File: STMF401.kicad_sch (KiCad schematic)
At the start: 26 parts, among them J6 Conn_01x04_Pin, U7 STM32F407VETx, Y1 X322525MQB4SI, Y2 SMD03215C2

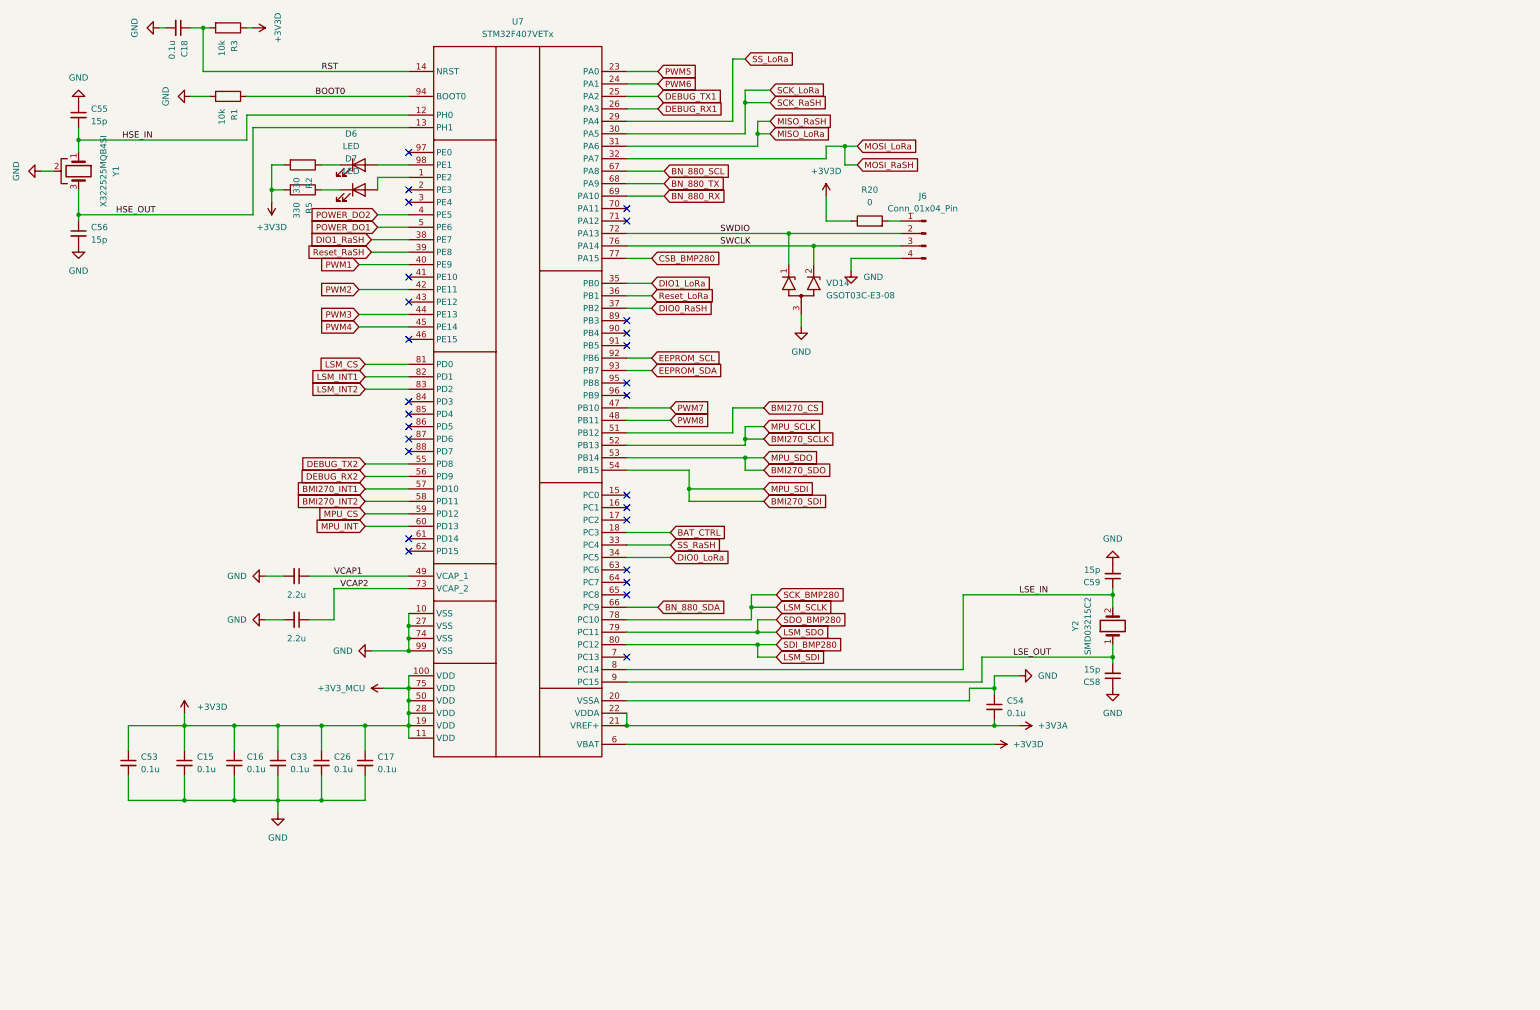
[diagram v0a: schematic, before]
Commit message: feat:убрал часть с батарейным питанием, убрал лишние элементы со старого проекта
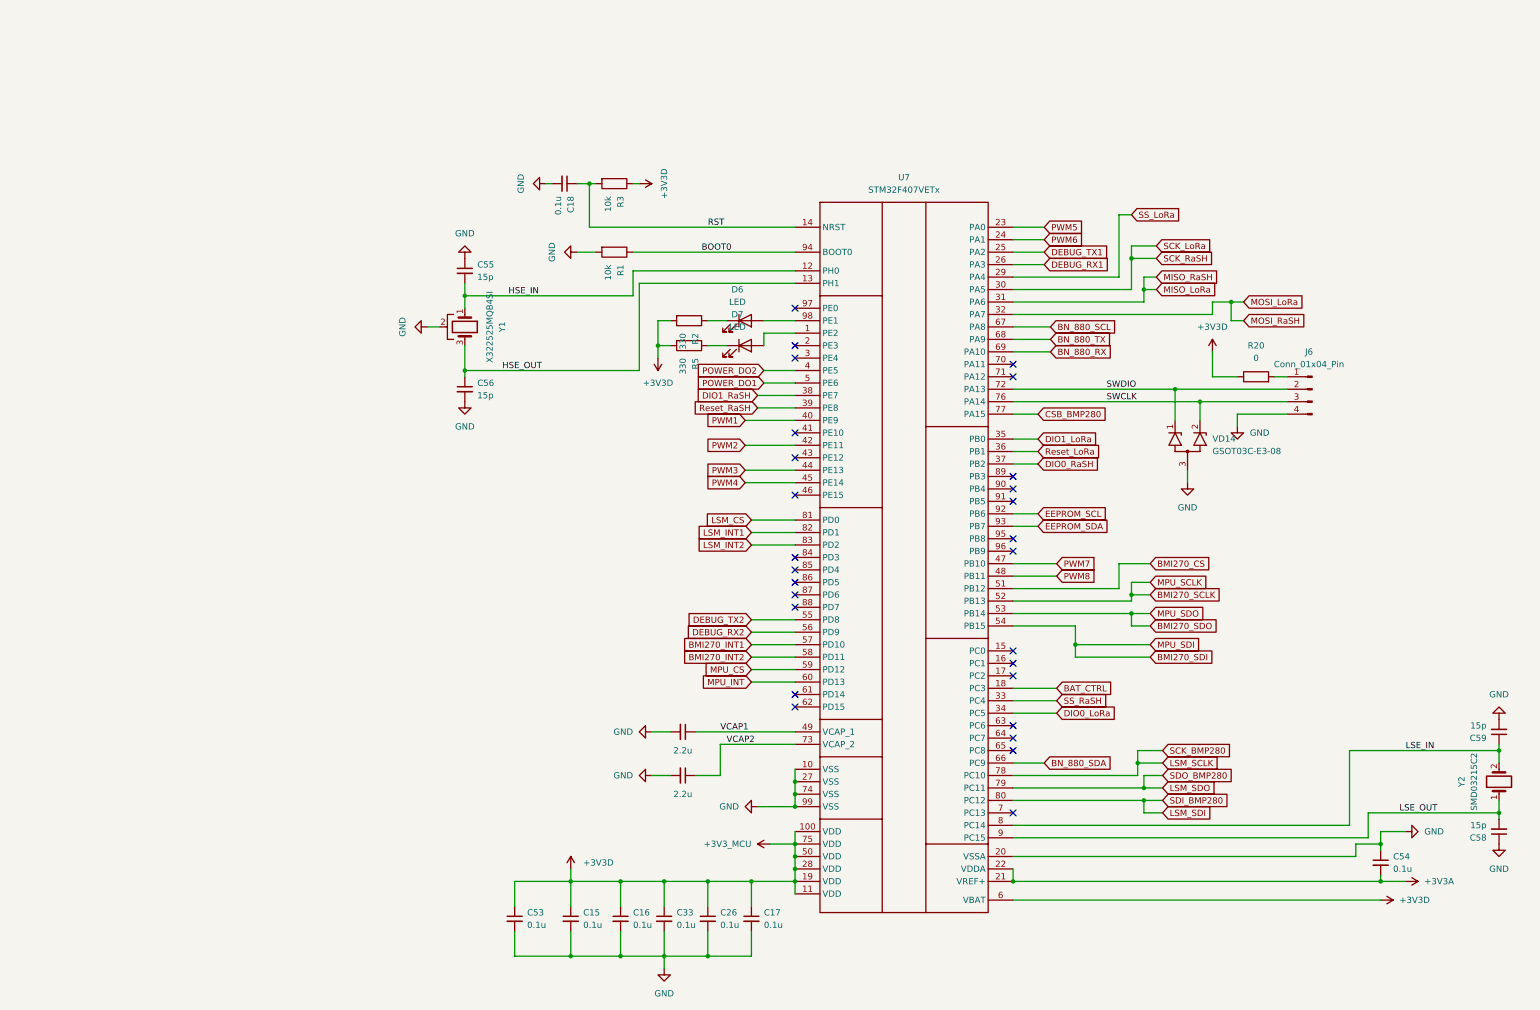
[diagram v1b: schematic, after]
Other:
- moved on the sheet: C15, C16, C17, C18, C26, C33, C53, C54, C55, C56, C58, C59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

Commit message: feat: добавлены глобальные линии связи, удалены линии связи со старого проекта
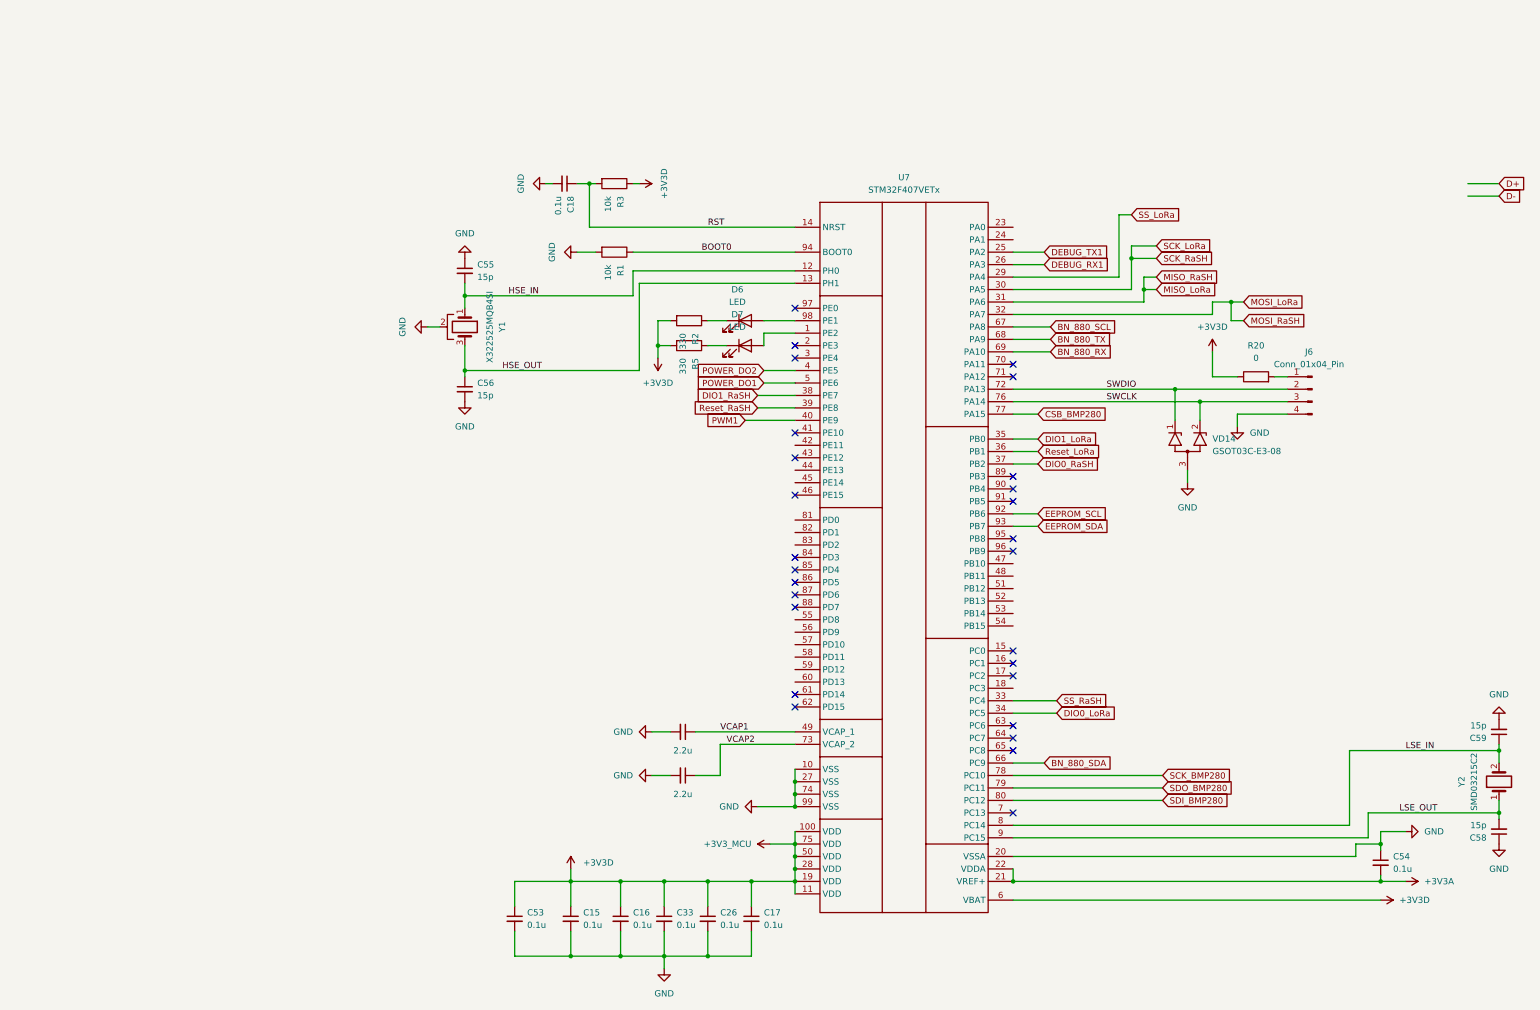
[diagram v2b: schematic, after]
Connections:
- net BAT_CTRL: no longer names the net of U7.18 (PC3)
- net BMI270_CS: no longer names the net of U7.51 (PB12)
- net BMI270_INT1: no longer names the net of U7.57 (PD10)
- net BMI270_INT2: no longer names the net of U7.58 (PD11)
- net BMI270_SCLK: no longer names the net of U7.52 (PB13)
- net BMI270_SDI: no longer names the net of U7.54 (PB15)
- net BMI270_SDO: no longer names the net of U7.53 (PB14)
- net DEBUG_RX2: no longer names the net of U7.56 (PD9)
- net DEBUG_TX2: no longer names the net of U7.55 (PD8)
- net LSM_CS: no longer names the net of U7.81 (PD0)
- net LSM_INT1: no longer names the net of U7.82 (PD1)
- net LSM_INT2: no longer names the net of U7.83 (PD2)
- net LSM_SCLK renamed SCK_BMP280
- net LSM_SDI renamed SDI_BMP280
- net LSM_SDO renamed SDO_BMP280
- net MPU_CS: no longer names the net of U7.59 (PD12)
- net MPU_INT: no longer names the net of U7.60 (PD13)
- net PWM2: no longer names the net of U7.42 (PE11)
- net PWM3: no longer names the net of U7.44 (PE13)
- net PWM4: no longer names the net of U7.45 (PE14)
- net PWM5: no longer names the net of U7.23 (PA0)
- net PWM6: no longer names the net of U7.24 (PA1)
- net PWM7: no longer names the net of U7.47 (PB10)
- net PWM8: no longer names the net of U7.48 (PB11)

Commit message: feat: добавлены светодиоды
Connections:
- no-connect marks 27 -> 0
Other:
- note added: "SPI3 (CH32V303)"
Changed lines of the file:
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@@
 	(generator_version "10.0")
 	(paper "A3")
+	(text "SPI3 (CH32V303)"
+		(exclude_from_sim no)
+		(at 277.368 173.99 0)
+		(effects
+			(font
+				(size 1.27 1.27)
+			)
+		)
+	)
 	(junction
 		(at 151.13 208.28)
@@
 		(color 0 0 0 0)
 	)
-	(no_connect
-		(at 177.8 137.16)
-	)
-	(no_connect
-		(at 177.8 127)
-	)
-	(no_connect
-		(at 222.25 110.49)
-	)
-	(no_connect
-		(at 222.25 125.73)
-	)
-	(no_connect
-		(at 222.25 179.07)
-	)
-	(no_connect
-		(at 177.8 101.6)
-	)
-	(no_connect
-		(at 222.25 161.29)
-	)
-	(no_connect
-		(at 177.8 106.68)
-	)
-	(no_connect
-		(at 177.8 76.2)
-	)
-	(no_connect
-		(at 222.25 163.83)
-	)
-	(no_connect
-		(at 222.25 123.19)
-	)
-	(no_connect
-		(at 177.8 154.94)
-	)
-	(no_connect
-		(at 222.25 166.37)
-	)
-	(no_connect
-		(at 222.25 148.59)
-	)
-	(no_connect
-		(at 177.8 157.48)
-	)
-	(no_connect
-		(at 177.8 83.82)
-	)
-	(no_connect
-		(at 177.8 132.08)
-	)
-	(no_connect
-		(at 177.8 134.62)
-	)
-	(no_connect
-		(at 222.25 151.13)
-	)
-	(no_connect
-		(at 222.25 146.05)
-	)
-	(no_connect
-		(at 177.8 114.3)
-	)
-	(no_connect
-		(at 177.8 129.54)
-	)
-	(no_connect
-		(at 222.25 113.03)
-	)
-	(no_connect
-		(at 222.25 87.63)
-	)
-	(no_connect
-		(at 222.25 90.17)
-	)
-	(no_connect
-		(at 177.8 86.36)
-	)
-	(no_connect
-		(at 222.25 115.57)
-	)
 	(wire

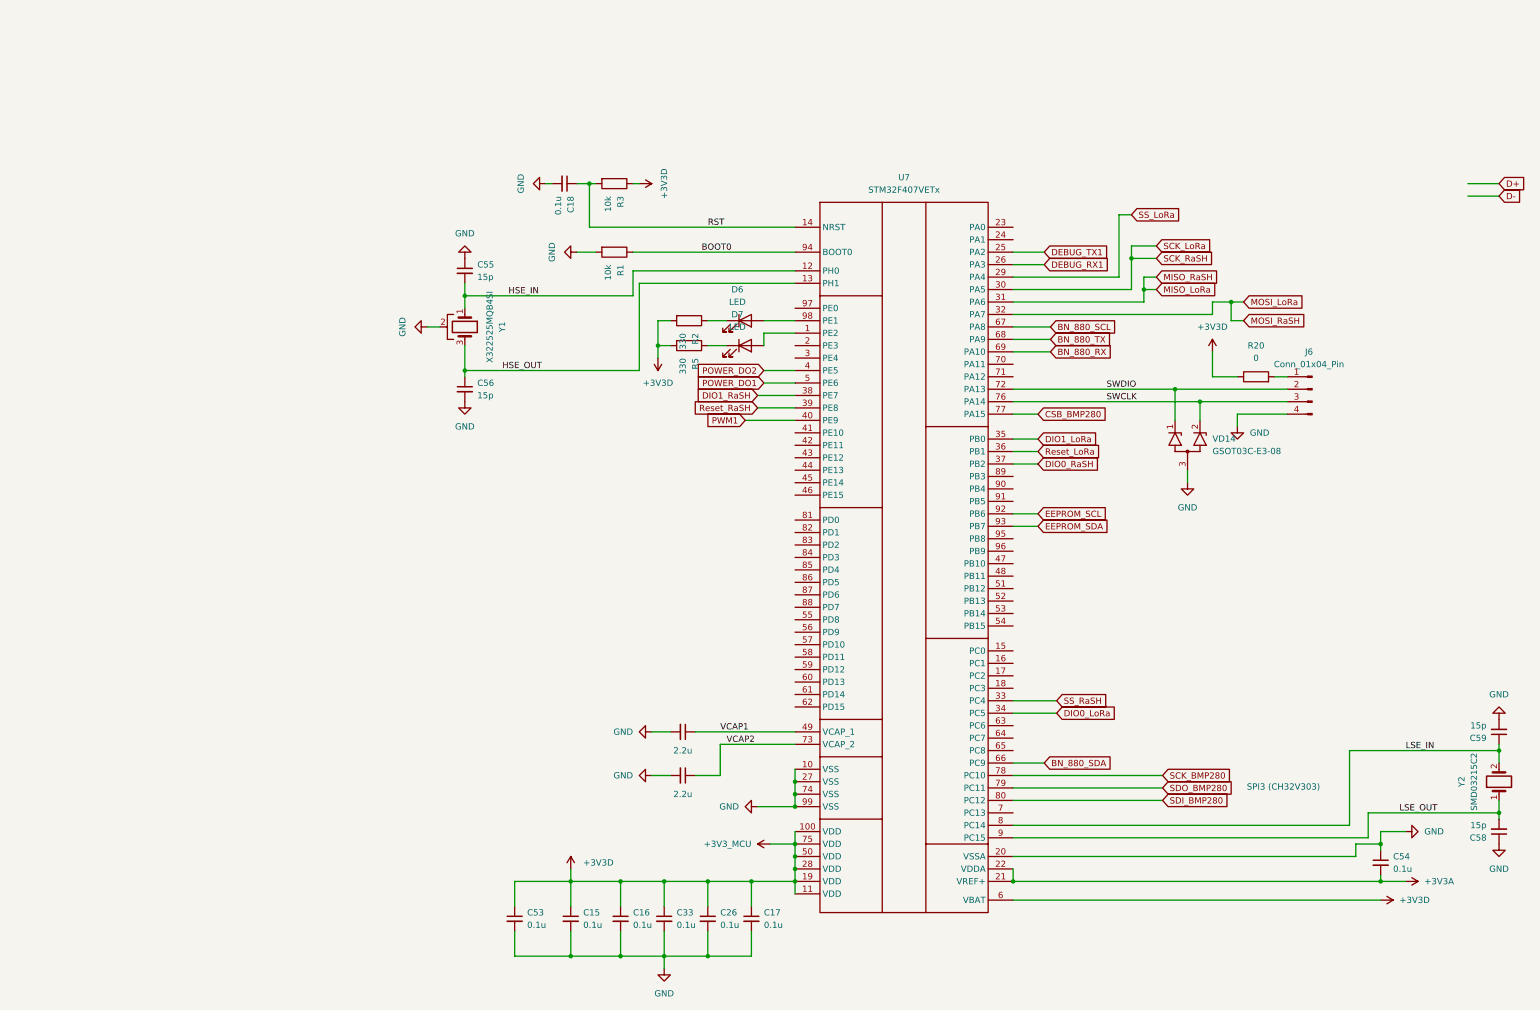
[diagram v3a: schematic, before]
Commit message: feat: добавлены связи цифровых линий с МК
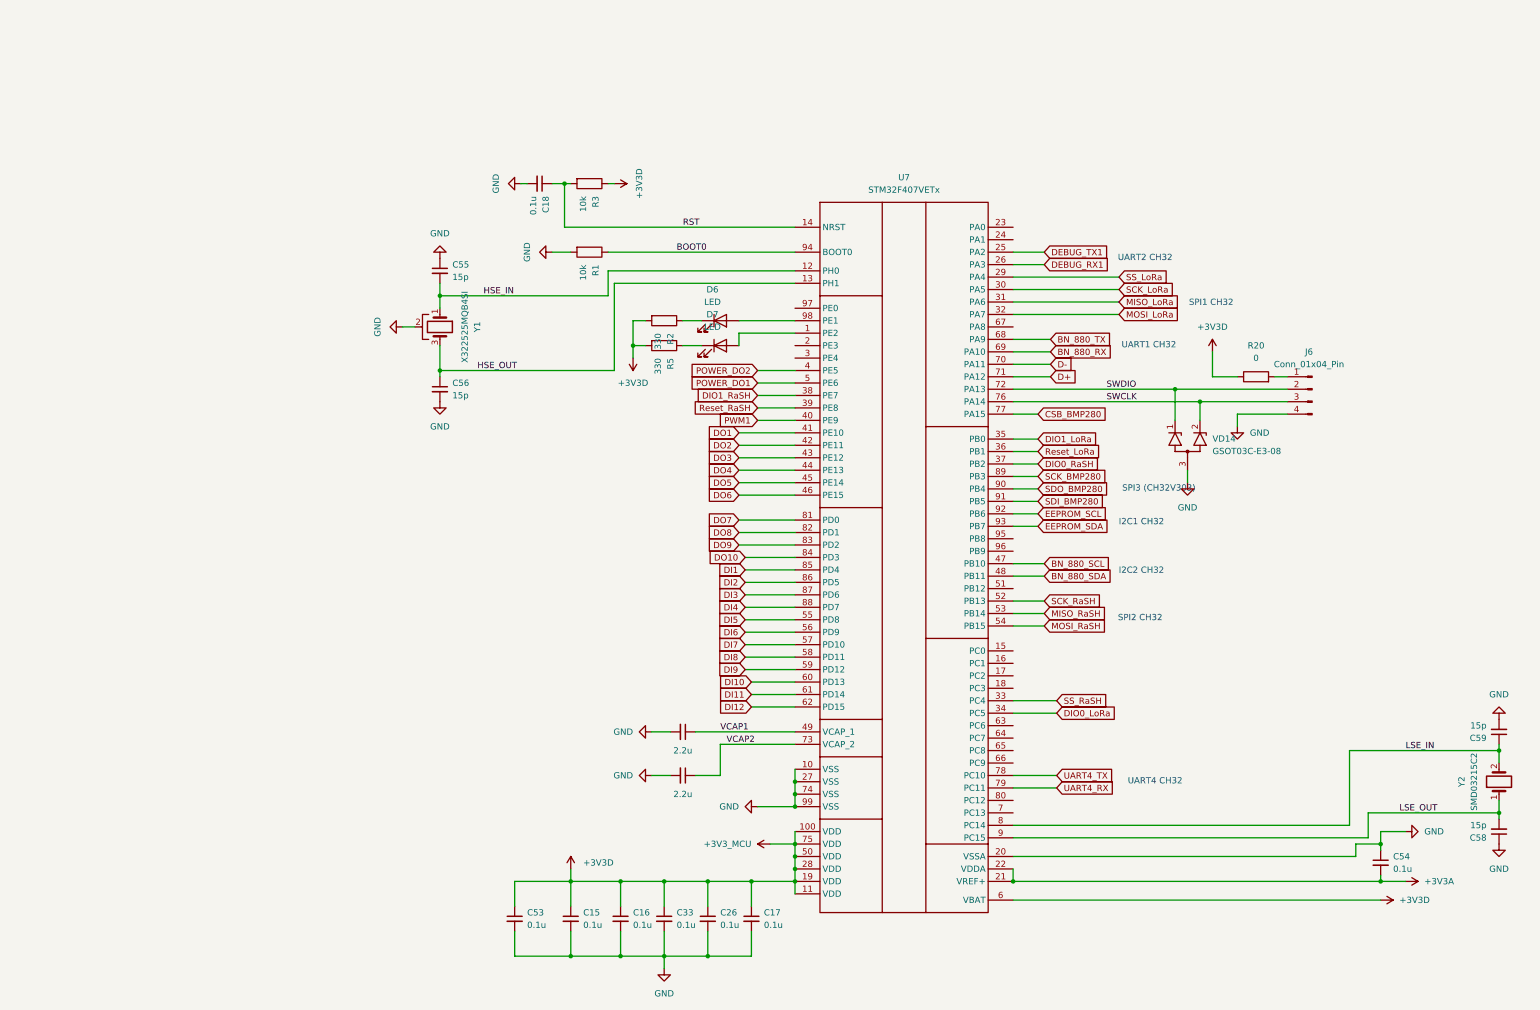
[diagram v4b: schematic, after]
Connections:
- net BN_880_SCL: now also U7.47 (PB10); no longer U7.67 (PA8)
- net BN_880_SDA: now also U7.48 (PB11); no longer U7.66 (PC9)
- net D+: now also U7.71 (PA12)
- net D-: now also U7.70 (PA11)
- net SCK_BMP280: now also U7.89 (PB3); no longer U7.78 (PC10)
- net SDI_BMP280: now also U7.91 (PB5); no longer U7.80 (PC12)
- net SDO_BMP280: now also U7.90 (PB4); no longer U7.79 (PC11)
- net DO1: now reaches U7.41 (PE10)
- net DO2: now reaches U7.42 (PE11)
- net DO3: now reaches U7.43 (PE12)
- net DO4: now reaches U7.44 (PE13)
- net DO5: now reaches U7.45 (PE14)
- net DO6: now reaches U7.46 (PE15)
- net SCK_RaSH: now reaches U7.52 (PB13)
- net MISO_RaSH: now reaches U7.53 (PB14)
- net MOSI_RaSH: now reaches U7.54 (PB15)
- net DI5: now reaches U7.55 (PD8)
- net DI6: now reaches U7.56 (PD9)
- net DI7: now reaches U7.57 (PD10)
- net DI8: now reaches U7.58 (PD11)
- net DI9: now reaches U7.59 (PD12)
- net DI10: now reaches U7.60 (PD13)
- net DI11: now reaches U7.61 (PD14)
- net DI12: now reaches U7.62 (PD15)
- net DO7: now reaches U7.81 (PD0)
- net DO8: now reaches U7.82 (PD1)
- net DO9: now reaches U7.83 (PD2)
- net DO10: now reaches U7.84 (PD3)
- net DI1: now reaches U7.85 (PD4)
- net DI2: now reaches U7.86 (PD5)
- net DI3: now reaches U7.87 (PD6)
- net DI4: now reaches U7.88 (PD7)
- new net UART4_RX: U7.79 (PC11)
- new net UART4_TX: U7.78 (PC10)
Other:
- note added: "I2C1 CH32"
- note added: "I2C2 CH32"
- note added: "SPI1 CH32"
- note added: "SPI2 CH32"
- note added: "UART1 CH32"
- note added: "UART2 CH32"
- note added: "UART4 CH32"
- moved on the sheet: C18, C55, C56, D6, D7, R1, R2, R3, R5, Y1

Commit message: feat: расположены основные узлы модуля на печатной плате
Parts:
- renumbered C18 to C14, C55 to C15, C56 to C16, C19 to C17, C59 to C18, C57 to C19, C58 to C20, C54 to C21, C53 to C22, C15 to C23, C16 to C24, C33 to C25, C17 to C27, D7 to D10, D6 to D9, R3 to R10, R1 to R11, R2 to R12, R5 to R13, R20 to R14, U7 to U3, VD14 to VD2

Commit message: feat: размешены все компоненты на печатной плате
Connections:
- net +3V3D is gone; now on net +3V3: C22.1, C23.1, C24.1, C25.1, C26.1, C27.1, R10.1, R12.2, R13.2, R14.1, U3.100 (VDD), U3.11 (VDD), U3.19 (VDD), U3.28 (VDD), U3.50 (VDD), U3.6 (VBAT), U3.75 (VDD)
- net +3V3A renamed +3V3

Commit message: feat: начата разводка сигнальных линий и линий питания
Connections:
- no-connect marks 0 -> 18
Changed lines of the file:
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@@
 		(color 0 0 0 0)
+	)
+	(no_connect
+		(at 222.25 62.23)
+	)
+	(no_connect
+		(at 222.25 59.69)
+	)
+	(no_connect
+		(at 222.25 168.91)
+	)
+	(no_connect
+		(at 222.25 148.59)
+	)
+	(no_connect
+		(at 222.25 123.19)
+	)
+	(no_connect
+		(at 177.8 76.2)
+	)
+	(no_connect
+		(at 222.25 125.73)
+	)
+	(no_connect
+		(at 222.25 179.07)
+	)
+	(no_connect
+		(at 177.8 86.36)
+	)
+	(no_connect
+		(at 177.8 83.82)
+	)
+	(no_connect
+		(at 222.25 146.05)
+	)
+	(no_connect
+		(at 222.25 161.29)
+	)
+	(no_connect
+		(at 222.25 163.83)
+	)
+	(no_connect
+		(at 222.25 80.01)
+	)
+	(no_connect
+		(at 222.25 176.53)
+	)
+	(no_connect
+		(at 222.25 166.37)
+	)
+	(no_connect
+		(at 222.25 151.13)
+	)
+	(no_connect
+		(at 222.25 153.67)
 	)
 	(wire
